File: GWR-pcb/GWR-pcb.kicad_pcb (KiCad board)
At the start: 2 copper layers, 69 x 39 mm, 43 parts, among them J1 Conn_01x04, J2 Conn_01x11, J3 Conn_01x10, J4 Conn_01x10, Q1 AO3400A, SW1 SW_DIP_x01, U1 AMS1117-1.5, U2 XIAO-ESP32-S3-Plus-SMD, U3 MAX98357A, U4 74AUP1G32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

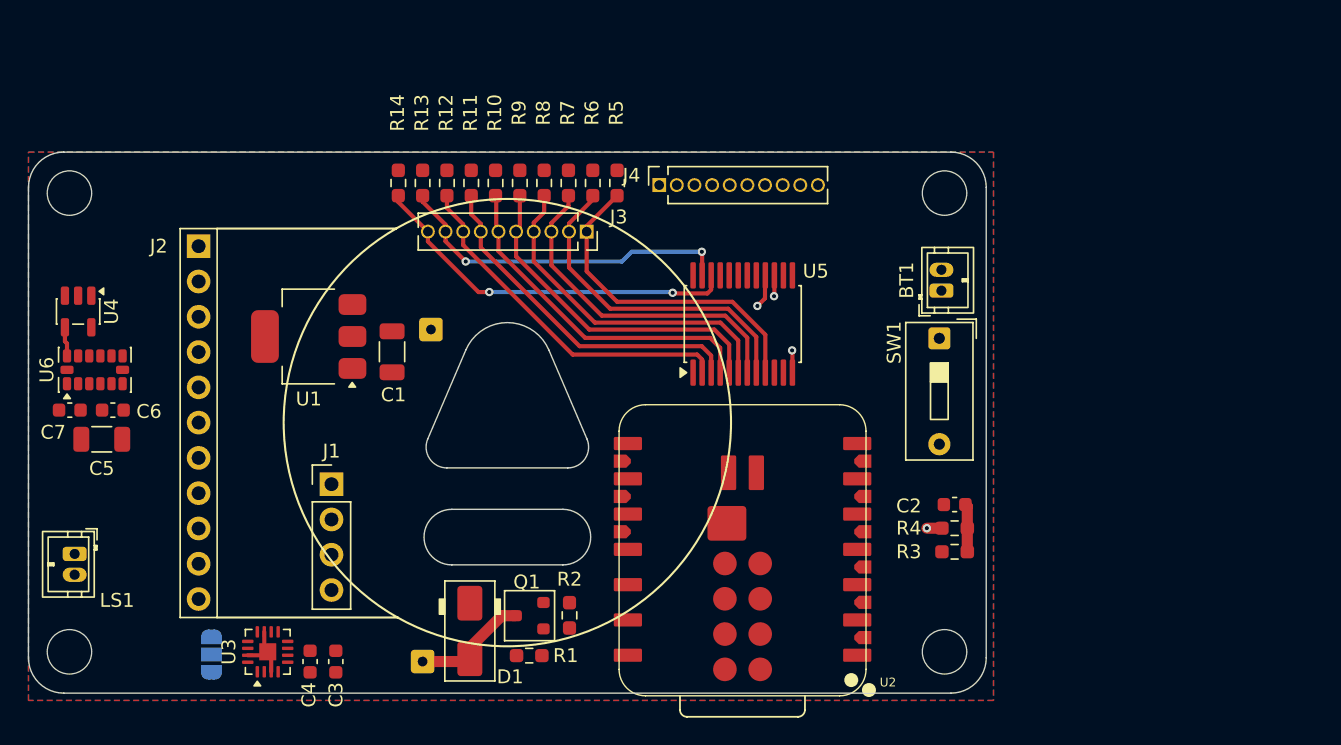
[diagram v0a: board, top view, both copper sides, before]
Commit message: update to use GPIO expander, minor fixes
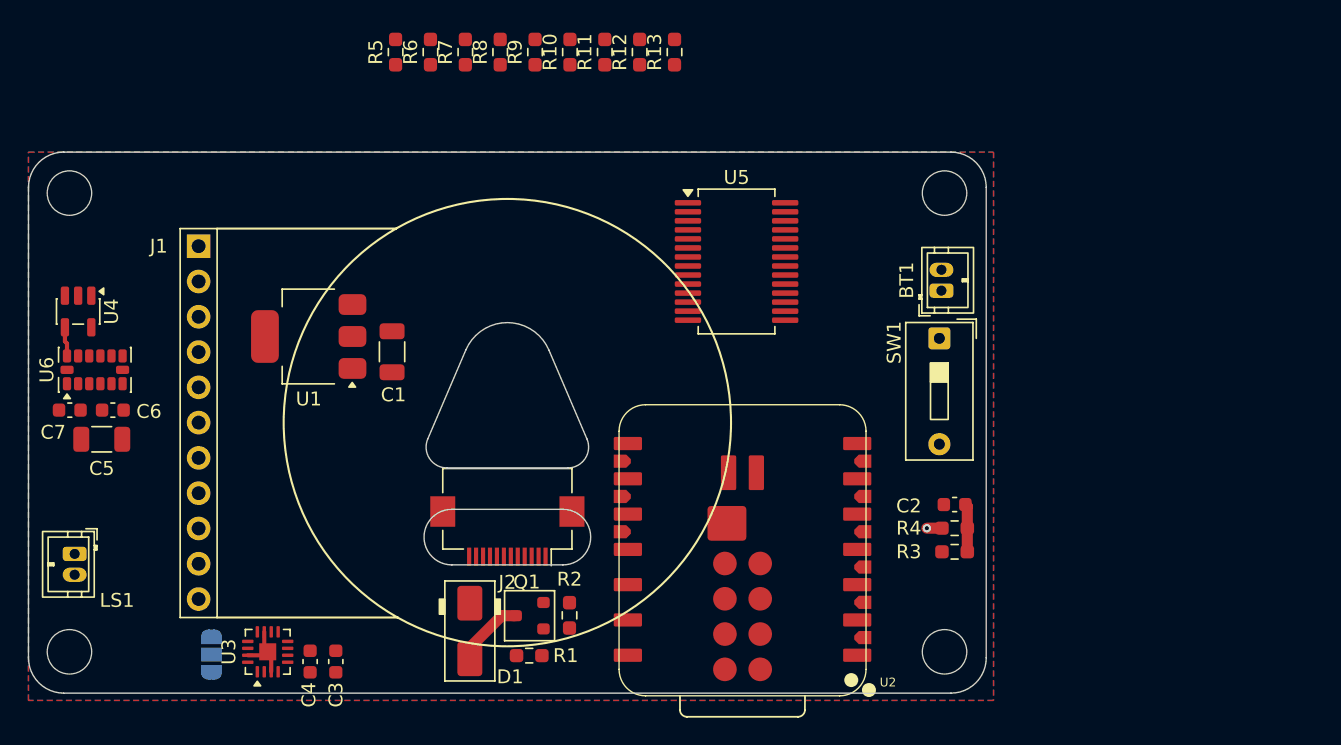
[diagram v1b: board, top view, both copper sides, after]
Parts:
- removed the J1 at (51.8, 53.9)
- removed J3, J4: Conn_01x10, Connector_PinSocket_1.27mm:PinSocket_1x10_P1.27mm_Vertical
- removed R14: 10k, Resistor_SMD:R_0603_1608Metric_Pad0.98x0.95mm_HandSolder
- removed TP1: MotorPlus, Connector_Wire:SolderWire-0.127sqmm_1x01_D0.48mm_OD1mm
- removed TP2: MotorMinus, Connector_Wire:SolderWire-0.127sqmm_1x01_D0.48mm_OD1mm
- added J2: Conn_01x12, Connector_FFC-FPC:Hirose_FH12-12S-0.5SH_1x12-1MP_P0.50mm_Horizontal, F.Cu at (64.5, 57.3)
- U5: value CD74HC4067SM96 -> MCP23S17x-x-SS; footprint Package_SO:SSOP-24_5.3x8.2mm_P0.65mm -> Package_SO:SSOP-28_5.3x10.2mm_P0.65mm
- moved R13 20.4 mm to (76.5, 22.8), turned to 90 degrees
- moved R5 18.5 mm to (56.4, 22.8), turned to 90 degrees
- moved R12 16.8 mm to (74.0, 22.8), turned to 90 degrees
- moved R6 15.0 mm to (58.9, 22.8), turned to 90 degrees
- moved R11 13.5 mm to (71.5, 22.8), turned to 90 degrees
- moved R7 12.0 mm to (61.5, 22.8), turned to 90 degrees
- moved R10 10.8 mm to (69.0, 22.8), turned to 90 degrees
- moved R8 9.94 mm to (64.0, 22.8), turned to 90 degrees
- moved R9 9.49 mm to (66.5, 22.8), turned to 90 degrees
- moved U5 4.52 mm to (81.0, 37.9), turned to 0 degrees
- renumbered J2 to J1
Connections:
- net Net-(D1-A) renamed /MOTOR_LOW
- net Net-(D1-K) renamed /MOTOR_HIGH
- R10 pad 2: /BUTTON_F -> /BUTTON_E
- R11 pad 2: /BUTTON_G -> /BUTTON_F
- R12 pad 2: /BUTTON_H -> /BUTTON_G
- R13 pad 2: /BUTTON_I -> /BUTTON_H
- R5 pad 2: /BUTTON_A -> /GPIOEXP_RST
- R6 pad 2: /BUTTON_B -> /BUTTON_A
- R7 pad 2: /BUTTON_C -> /BUTTON_B
- R8 pad 2: /BUTTON_D -> /BUTTON_C
- R9 pad 2: /BUTTON_E -> /BUTTON_D
- U2 pad 2: /SIG_MUX_COM -> /TFT_CS
- U2 pad 21: /HX710_OUT -> /ADXL_CS
- U2 pad 23: /HX710_SCK -> unconnected-(U2-GPIO13_DVP_PCLK_SPI_SCK1-Pad23)
- U2 pad 3: /SIG_DEMUX_A -> /GPIOEXP_CS
- U2 pad 4: /SIG_DEMUX_B -> /GPIOEXP_INTA
- U2 pad 5: /SIG_DEMUX_C -> /GPIOEXP_RST
- U2 pad 6: /SIG_DEMUX_D -> /SD_CS
- U2 pad 7: unconnected-(U2-GPIO43_D6_TX-Pad7) -> /SIG_VIBRATION
- U5 pad 1: /SIG_MUX_COM -> unconnected-(U5-GPB0-Pad1)
- U5 pad 10: /SIG_DEMUX_A -> GND
- U5 pad 11: /SIG_DEMUX_B -> /GPIOEXP_CS
- U5 pad 12: GND -> /ESP_SCK
- U5 pad 13: /SIG_DEMUX_D -> /ESP_MOSI
- U5 pad 14: /SIG_DEMUX_C -> /ESP_MISO
- U5 pad 16: /SIG_VIBRATION -> GND
- U5 pad 17: unconnected-(U5-I14-Pad17) -> GND
- U5 pad 18: unconnected-(U5-I13-Pad18) -> /GPIOEXP_RST
- U5 pad 19: /ADXL_CS -> unconnected-(U5-INTB-Pad19)
- U5 pad 2: /BUTTON_H -> unconnected-(U5-GPB1-Pad2)
- U5 pad 20: /SD_CS -> /GPIOEXP_INTA
- U5 pad 21: /TFT_CS -> /BUTTON_A
- U5 pad 22: /BUTTON_J -> /BUTTON_B
- U5 pad 23: /BUTTON_I -> /BUTTON_C
- U5 pad 24: +3V3 -> /BUTTON_D
- U5 pad 3: /BUTTON_G -> unconnected-(U5-GPB2-Pad3)
- U5 pad 4: /BUTTON_F -> unconnected-(U5-GPB3-Pad4)
- U5 pad 5: /BUTTON_E -> unconnected-(U5-GPB4-Pad5)
- U5 pad 6: /BUTTON_D -> unconnected-(U5-GPB5-Pad6)
- U5 pad 7: /BUTTON_C -> unconnected-(U5-GPB6-Pad7)
- U5 pad 8: /BUTTON_B -> unconnected-(U5-GPB7-Pad8)
- U5 pad 9: /BUTTON_A -> +3V3
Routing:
- net /BUTTON_J: track 27.3 -> 0.00 mm, vias 2 -> 0
- net /BUTTON_H: track 25.6 -> 0.00 mm
- net /BUTTON_G: track 25.0 -> 0.00 mm
- net /BUTTON_I: track 25.0 -> 0.00 mm, vias 2 -> 0
- net /BUTTON_F: track 24.7 -> 0.00 mm
- net /BUTTON_E: track 24.5 -> 0.00 mm
- net /BUTTON_D: track 24.4 -> 0.00 mm
- net /BUTTON_C: track 24.3 -> 0.00 mm
- net /BUTTON_B: track 24.0 -> 0.00 mm
- net /BUTTON_A: track 23.8 -> 0.00 mm
- net /MOTOR_LOW: track 8.54 -> 5.34 mm
- net GND: track 8.83 -> 5.71 mm, vias 3 -> 1
- net /SIG_VIBRATION: track 2.44 -> 0.00 mm, vias 1 -> 0

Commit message: standardize port to match 3D; panelize daughterboard
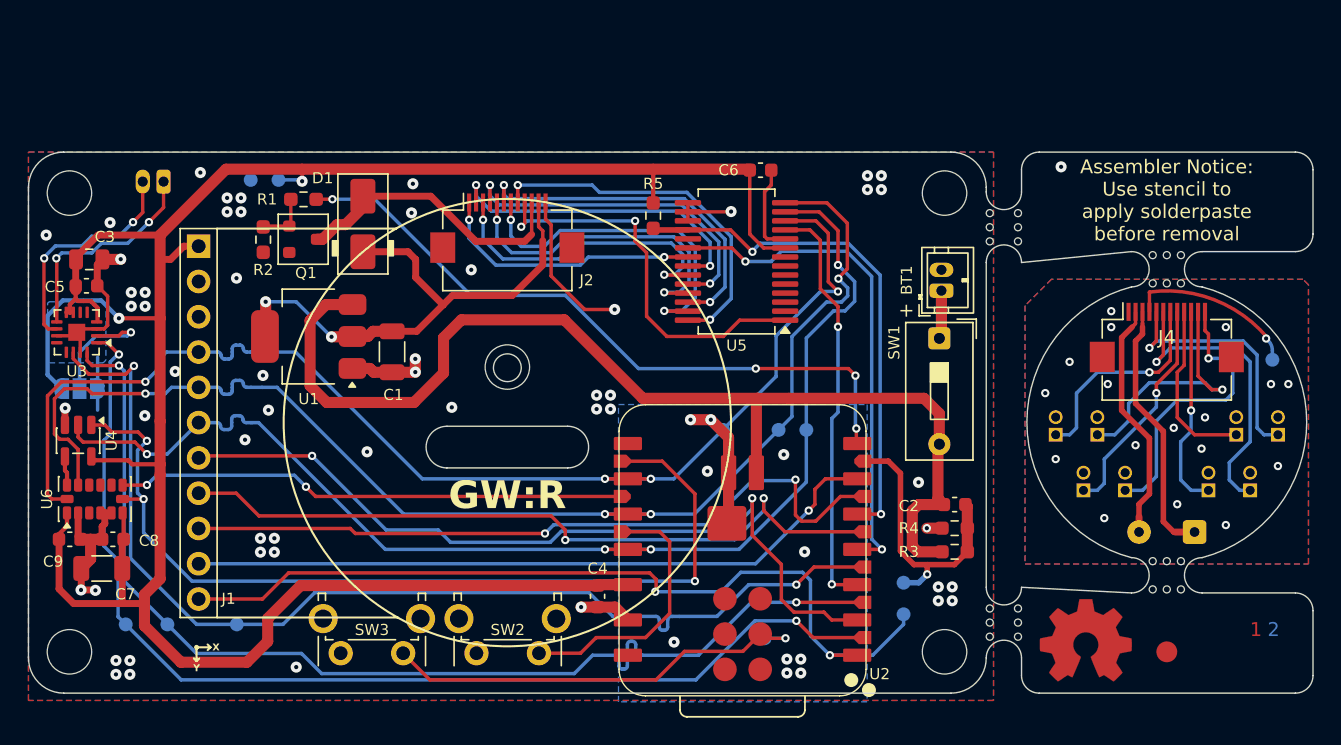
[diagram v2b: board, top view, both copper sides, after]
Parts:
- removed R10, R11, R12, R13, R6, R7, R8, R9: 10k, Resistor_SMD:R_0603_1608Metric_Pad0.98x0.95mm_HandSolder
- added C4: 1u, Capacitor_SMD:C_0603_1608Metric, F.Cu at (71.0, 62.0)
- added C6: 100n, Capacitor_SMD:C_0603_1608Metric, F.Cu at (82.7, 31.3)
- added H5: MountingHole, MountingHole:MountingHole_3.2mm_M3_DIN965, F.Cu at (64.5, 45.5)
- added J10: Conn_01x02, Connector_PinHeader_1.27mm:PinHeader_1x02_P1.27mm_Vertical, B.Cu at (104.0, 50.4)
- added J11: Conn_01x02, Connector_PinHeader_1.27mm:PinHeader_1x02_P1.27mm_Vertical, B.Cu at (118.0, 54.4)
- added J12: Conn_01x02, Connector_PinHeader_1.27mm:PinHeader_1x02_P1.27mm_Vertical, B.Cu at (120.0, 50.4)
- added J3: Conn_01x02, Connector_Wire:SolderWire-0.15sqmm_1x02_P4mm_D0.5mm_OD1.5mm, B.Cu at (114.0, 57.4)
- added J4: Conn_01x12, Connector_FFC-FPC:Hirose_FH12-12S-0.5SH_1x12-1MP_P0.50mm_Horizontal, F.Cu at (112.0, 43.4)
- added J5: Conn_01x02, Connector_PinHeader_1.27mm:PinHeader_1x02_P1.27mm_Vertical, B.Cu at (109.0, 54.4)
- added J6: Conn_01x02, Connector_PinHeader_1.27mm:PinHeader_1x02_P1.27mm_Vertical, B.Cu at (107.0, 50.4)
- added J7: Conn_01x02, Connector_PinHeader_1.27mm:PinHeader_1x02_P1.27mm_Vertical, B.Cu at (115.0, 54.4)
- added J8: Conn_01x02, Connector_PinHeader_1.27mm:PinHeader_1x02_P1.27mm_Vertical, B.Cu at (117.0, 50.4)
- added J9: Conn_01x02, Connector_PinHeader_1.27mm:PinHeader_1x02_P1.27mm_Vertical, B.Cu at (106.0, 54.4)
- added REF**: Mousebites OSHPARK Panel, glibri:Mousebites OSHPARK Panel, F.Cu at (99.0, 38.0)
- added REF**: Mousebites OSHPARK Panel, glibri:Mousebites OSHPARK Panel, F.Cu at (109.4, 59.2)
- added REF**: Mousebites OSHPARK Panel, glibri:Mousebites OSHPARK Panel, F.Cu at (109.4, 37.2)
- added REF**: Fiducial_1.5mm_Mask3mm, Fiducial:Fiducial_1.5mm_Mask3mm, F.Cu at (112.0, 66.0)
- added REF**: LayerMarker_2_3.81x2.54mm_TextH1mm_P1.27mm, Symbol:LayerMarker_2_3.81x2.54mm_TextH1mm_P1.27mm, F.Cu at (118.4, 65.6)
- added REF**: Mousebites OSHPARK Panel, glibri:Mousebites OSHPARK Panel, F.Cu at (99.0, 66.4)
- added REF**: OSHW-Symbol_6.7x6mm_Copper, Symbol:OSHW-Symbol_6.7x6mm_Copper, F.Cu at (106.1, 65.2)
- added REF**: Smolhaj_Scale_0.1, glibri:smallhaj, B.Cu at (104.6, 34.2)
- added SW2: Angled_Mode, Button_Switch_THT:SW_Tactile_SPST_Angled_PTS645Vx83-2LFS, F.Cu at (66.8, 66.1)
- added SW3: Angled_RST, Button_Switch_THT:SW_Tactile_SPST_Angled_PTS645Vx83-2LFS, F.Cu at (57.0, 66.1)
- added TP1: 3V3, TestPoint:TestPoint_Pad_D1.0mm, B.Cu at (48.0, 32.0)
- added TP10: BCLK, TestPoint:TestPoint_Pad_D1.0mm, B.Cu at (40.0, 64.0)
- added TP11: LRCLK, TestPoint:TestPoint_Pad_D1.0mm, B.Cu at (45.0, 64.0)
- added TP12: GND, TestPoint:TestPoint_Pad_D1.0mm, B.Cu at (119.5, 45.0)
- added TP2: GND, TestPoint:TestPoint_Pad_D1.0mm, B.Cu at (46.0, 32.0)
- added TP3: VBATDIV, TestPoint:TestPoint_Pad_D1.0mm, B.Cu at (93.0, 61.0)
- added TP4: RST, TestPoint:TestPoint_Pad_D1.0mm, B.Cu at (83.0, 65.0)
- added TP5: MOSI, TestPoint:TestPoint_Pad_D1.0mm, B.Cu at (86.0, 50.0)
- added TP6: MISO, TestPoint:TestPoint_Pad_D1.0mm, B.Cu at (84.0, 50.0)
- added TP7: SCK, TestPoint:TestPoint_Pad_D1.0mm, B.Cu at (80.0, 50.0)
- added TP8: BLPWM, TestPoint:TestPoint_Pad_D1.0mm, B.Cu at (93.0, 63.3)
- added TP9: DIN, TestPoint:TestPoint_Pad_D1.0mm, B.Cu at (37.0, 64.0)
- C3: footprint Capacitor_SMD:C_0603_1608Metric -> Capacitor_SMD:C_0805_2012Metric
- LS1: moved to B.Cu
- moved R1 36.6 mm to (49.8, 33.4), turned to 180 degrees
- moved R2 34.9 mm to (46.9, 36.3), turned to -90 degrees
- moved C3 34.0 mm to (34.4, 37.7), turned to 0 degrees
- moved Q1 31.6 mm to (49.8, 36.3), turned to 0 degrees
- moved C5 31.5 mm to (34.2, 39.6), turned to 0 degrees
- moved D1 30.3 mm to (54.1, 35.2), turned to 90 degrees
- moved LS1 27.6 mm to (39.7, 32.1), turned to 180 degrees
- moved U3 26.8 mm to (33.5, 43.0), turned to 180 degrees
- moved R5 22.0 mm to (75.0, 34.6), turned to -90 degrees
- moved J2 21.8 mm to (64.5, 35.5), turned to 0 degrees
- moved JP1 21.4 mm to (33.7, 47.0), turned to 180 degrees
- moved C7 9.30 mm to (35.3, 60.0)
- moved U6 9.30 mm to (34.8, 55.0)
- moved C8 9.30 mm to (36.1, 57.9)
- moved C9 9.30 mm to (33.0, 57.9)
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- renumbered C4 to C5, C5 to C7, C6 to C8, C7 to C9
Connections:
- net Net-(JP1-C) renamed /AUDIO_GAIN
- net Net-(Q1-G) renamed /SIG_QMOTOR
- net Net-(U3-OUTN) renamed /AUDIO_-
- net Net-(U3-OUTP) renamed /AUDIO_+
- J2 pad 9: unconnected-(J2-Pin_9-Pad9) -> /SIG_RESERVED1
- U2 pad 23: unconnected-(U2-GPIO13_DVP_PCLK_SPI_SCK1-Pad23) -> /SIG_SW_MODE
- U2 pad 26: unconnected-(U2-EN-Pad26) -> /SIG_SW_RST
- U5 pad 1: unconnected-(U5-GPB0-Pad1) -> /SIG_RESERVED1
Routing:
- net +3V3: track 0.00 -> 181.3 mm, vias 0 -> 2
- net /ESP_MISO: track 0.00 -> 94.1 mm, vias 0 -> 4
- net /ESP_SCK: track 0.00 -> 90.9 mm, vias 0 -> 4
- net /ESP_MOSI: track 0.00 -> 90.0 mm, vias 0 -> 4
- net /VBAT: track 0.00 -> 80.2 mm
- net /I2S_BCLK: track 0.00 -> 80.1 mm, vias 0 -> 2
- net /I2S_DIN: track 0.00 -> 79.5 mm, vias 0 -> 2
- net /I2S_LRCLK: track 0.00 -> 78.9 mm, vias 0 -> 2
- net /ADXL_CS: track 0.00 -> 66.7 mm, vias 0 -> 3
- net GND: track 5.71 -> 70.4 mm, vias 1 -> 82
- net /TFT_BL_PWM: track 0.00 -> 61.7 mm, vias 0 -> 2
- net /TFT_CS: track 0.00 -> 58.5 mm, vias 0 -> 2
- net /MOTOR_HIGH: track 0.00 -> 57.0 mm, vias 0 -> 2
- net /TFT_DC: track 0.00 -> 53.0 mm, vias 0 -> 2
- net /TFT_RST: track 0.00 -> 52.9 mm, vias 0 -> 2
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- added copper zone on B.Cu, net (none)
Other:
- board size 69 x 39 mm -> 92.5 x 39 mm
- board text added: "+"
- board text added: "0"
- board text added: "1"
- board text added: "2"
- board text added: "3"
- board text added: "4"
- board text added: "5"
- board text added: "6"
- board text added: "Assembler Notice: Use stencil to apply solderpaste before removal"
- board text added: "GW:R"
- board text added: "R"
- board text added: "Rev. A"
- board text added: "X"
- board text added: "Y"
